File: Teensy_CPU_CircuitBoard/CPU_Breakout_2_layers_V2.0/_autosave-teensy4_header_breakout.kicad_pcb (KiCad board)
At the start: 2 copper layers, 255 x 155.7 mm, 33 parts, among them U1 MCP2542WFDxMF, U2 NUCLEO-H745ZI-Q, U3 MCP2542WFDxMF

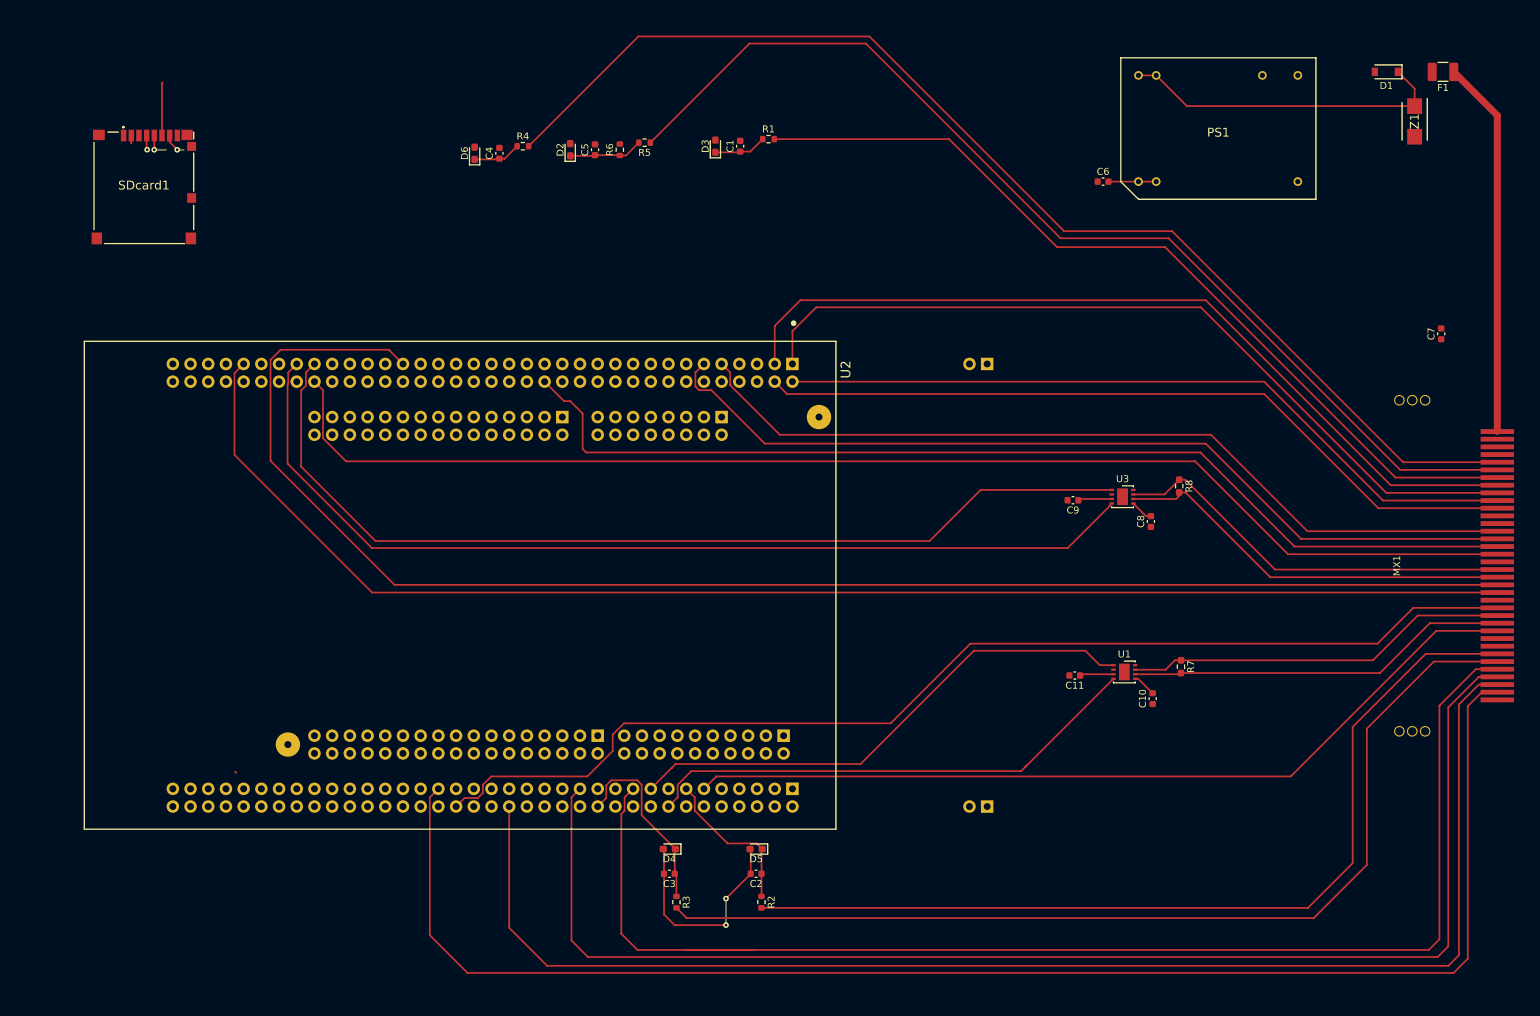
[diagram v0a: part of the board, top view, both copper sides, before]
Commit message: PCB trace 1.0V
Har ikke lagt til spenningsforsyning til sensorene eller GND. Dessuten har jeg satt connectoren feil vei
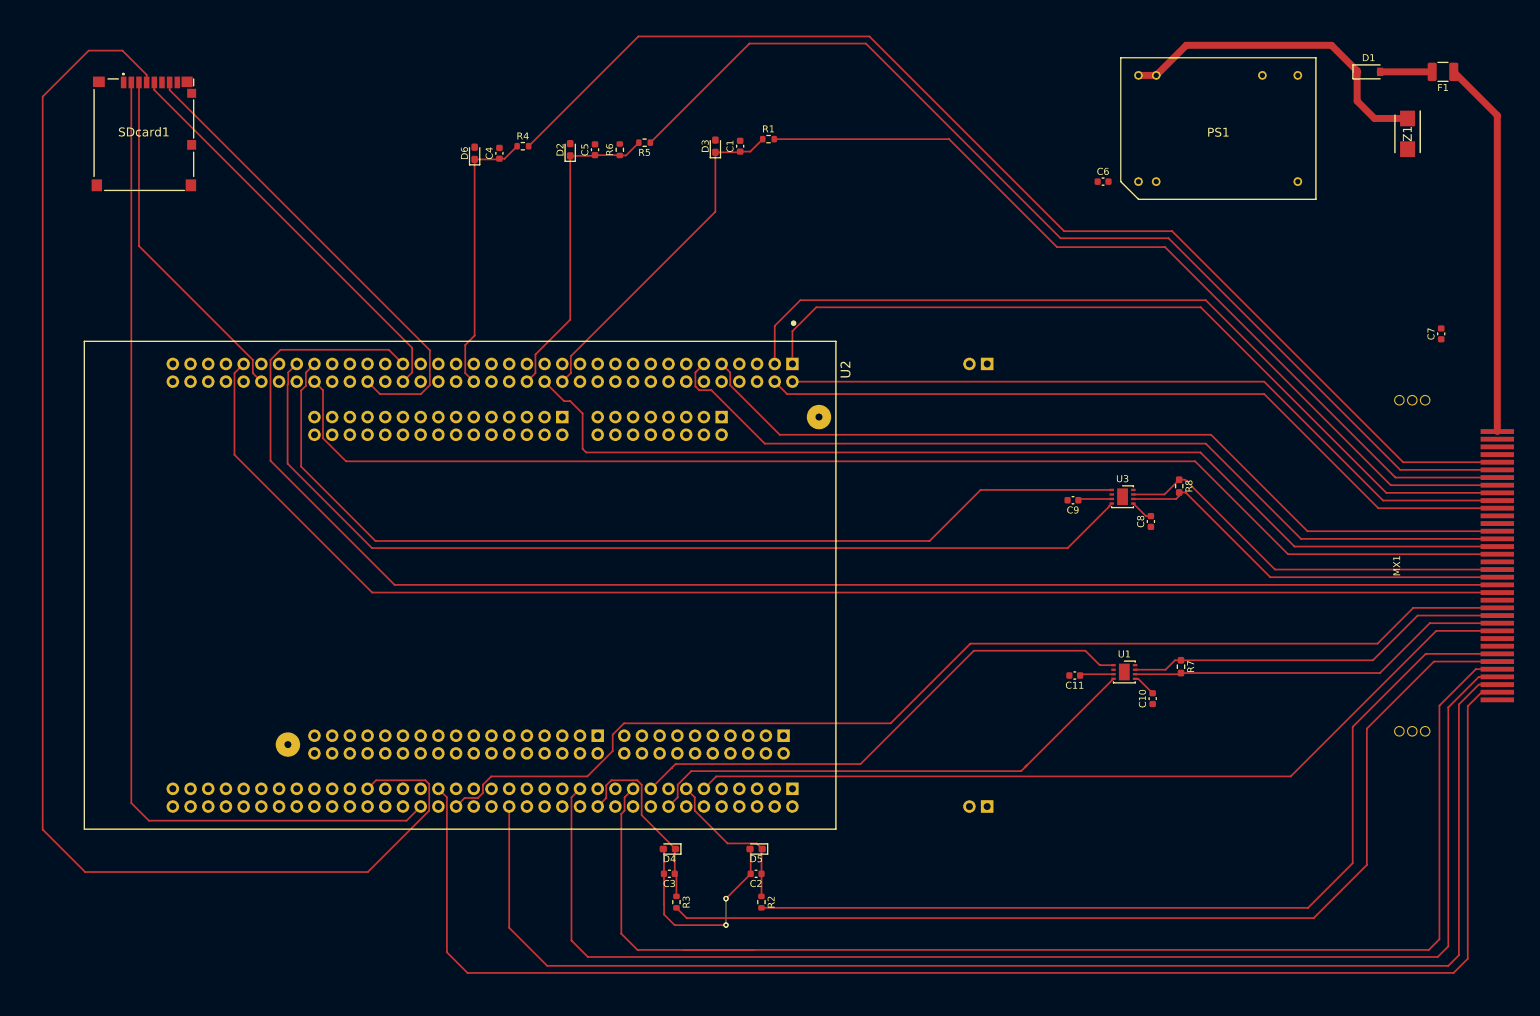
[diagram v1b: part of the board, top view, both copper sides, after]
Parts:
- moved SDcard1 7.62 mm to (44.5, 33.5)
- moved D1 2.54 mm to (227.3, 32.5), turned to 0 degrees
- moved Z1 2.05 mm to (232.9, 41.4)
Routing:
- net +3V3: track 8.70 -> 207.0 mm, vias 1 -> 0
- net SD-CS: track 1.36 -> 146.8 mm
- net SD-MISO: track 3.42 -> 69.1 mm, vias 1 -> 0
- net SD-SCK: track 3.74 -> 58.8 mm, vias 1 -> 0
- net SD-MOSI: track 0.00 -> 50.2 mm
- net SusDipsFiltered-FR: track 7.58 -> 49.6 mm
- net ClutchPSFiltered: track 10.7 -> 45.6 mm
- net SusDipsFiltered-RL: track 6.88 -> 39.8 mm
- net GND: track 39.0 -> 31.4 mm
- net Net-(D1-Pad2): track 0.00 -> 7.47 mm
- net Net-(C6-Pad2): track 6.84 -> 0.00 mm
- net WSHE-RR: track 214.8 -> 213.8 mm
